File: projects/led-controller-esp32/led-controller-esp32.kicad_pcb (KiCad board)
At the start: 2 copper layers, 49.5 x 41 mm, 9 parts, among them J1 Conn_01x02, J2 LED PIGTAIL, U1 XIAO ESP32C3, U2 DC Buck 5V

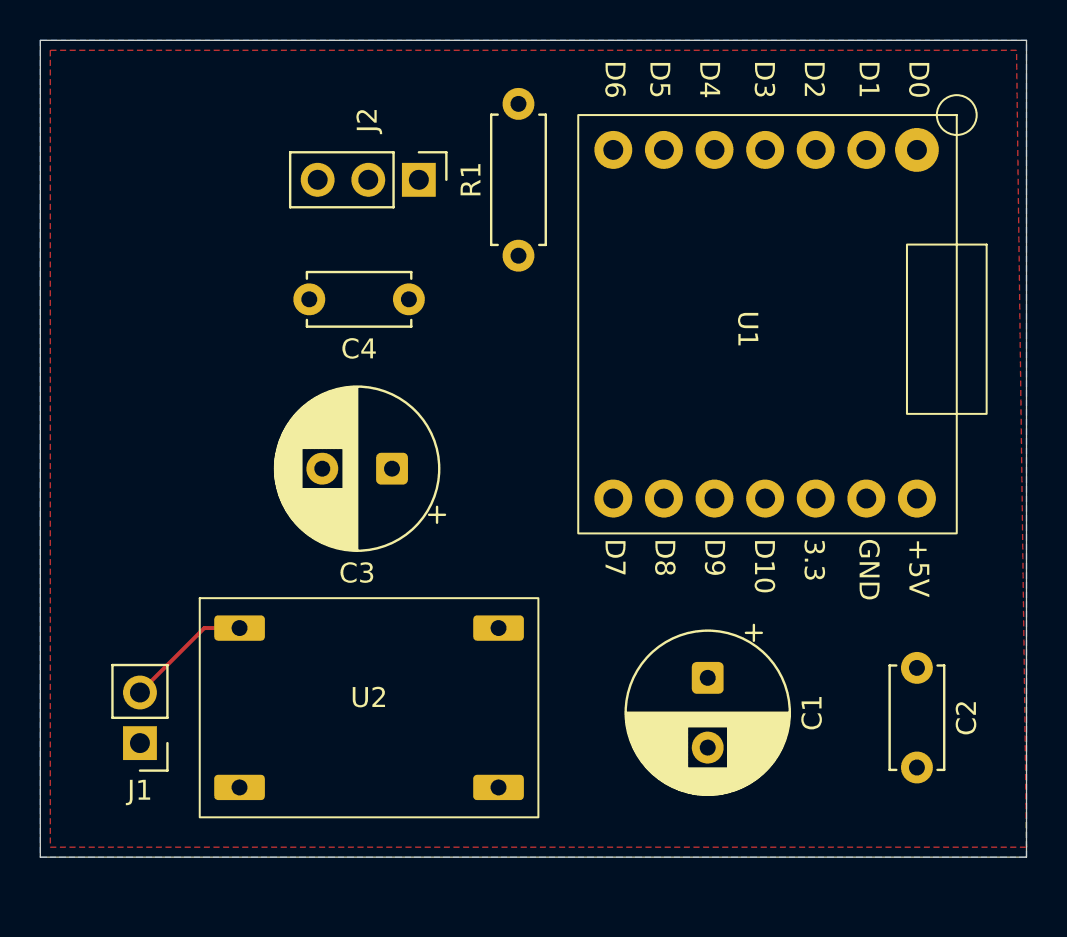
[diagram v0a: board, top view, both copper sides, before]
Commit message: use standard 2 screw terminal and other tidy ups
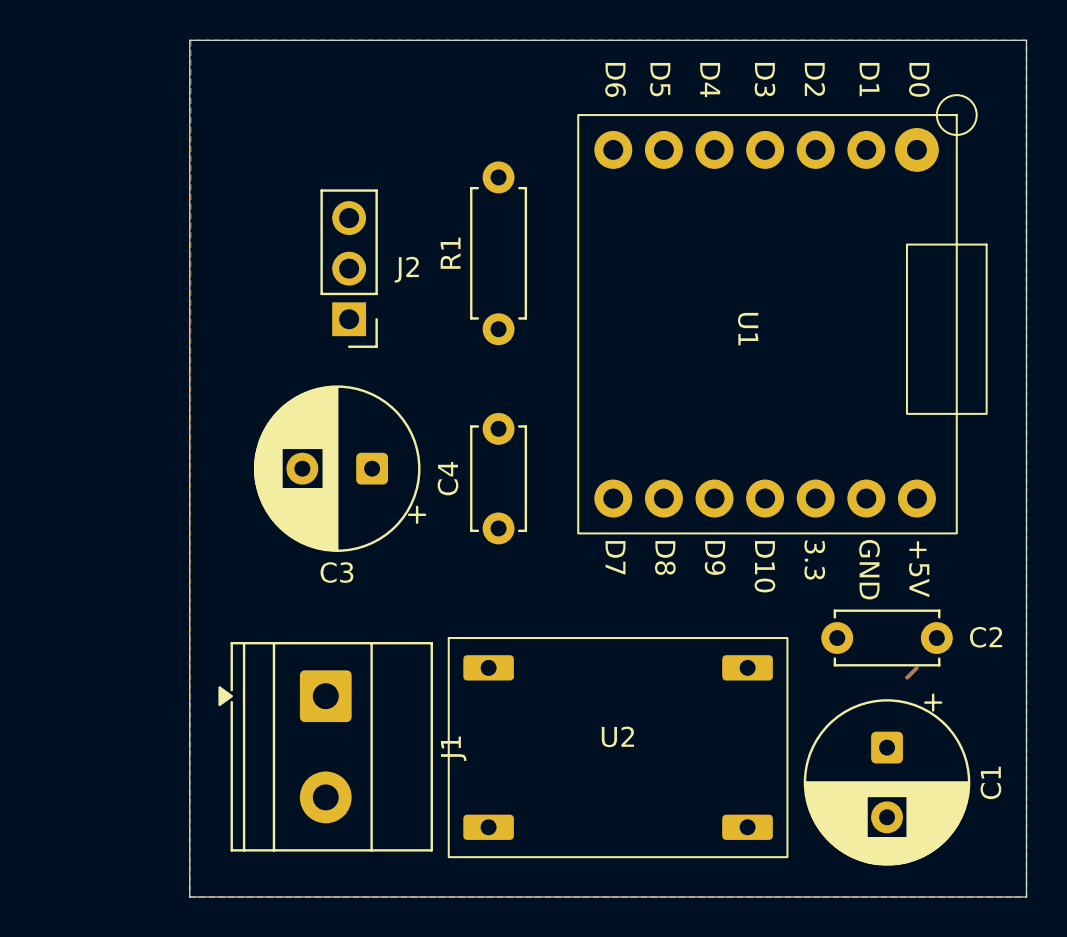
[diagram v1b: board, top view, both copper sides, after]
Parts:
- J1: value Conn_01x02 -> Screw_Terminal_01x02; footprint Connector_PinHeader_2.54mm:PinHeader_1x02_P2.54mm_Vertical -> TerminalBlock_Phoenix:TerminalBlock_Phoenix_MKDS-1,5-2-5.08_1x02_P5.08mm_Horizontal
- moved U2 12.7 mm to (106.0, 88.5)
- moved C4 12.3 mm to (100.0, 77.5), turned to 90 degrees
- moved C1 9.66 mm to (119.5, 88.5)
- moved J1 9.62 mm to (91.3, 85.9), turned to -90 degrees
- moved J2 7.83 mm to (92.5, 67.0), turned to 180 degrees
- moved C2 4.27 mm to (117.0, 83.0), turned to 0 degrees
- moved R1 3.82 mm to (100.0, 67.5)
- moved C3 1.00 mm to (93.7, 74.5)
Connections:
- J1 pad 1: GND -> +Vin
- J1 pad 2: +Vin -> GND
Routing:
- net +Vin: track 6.34 -> 0.00 mm
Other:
- board size 49.5 x 41 mm -> 42 x 43 mm

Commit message: label terminal blocks and other cleanups
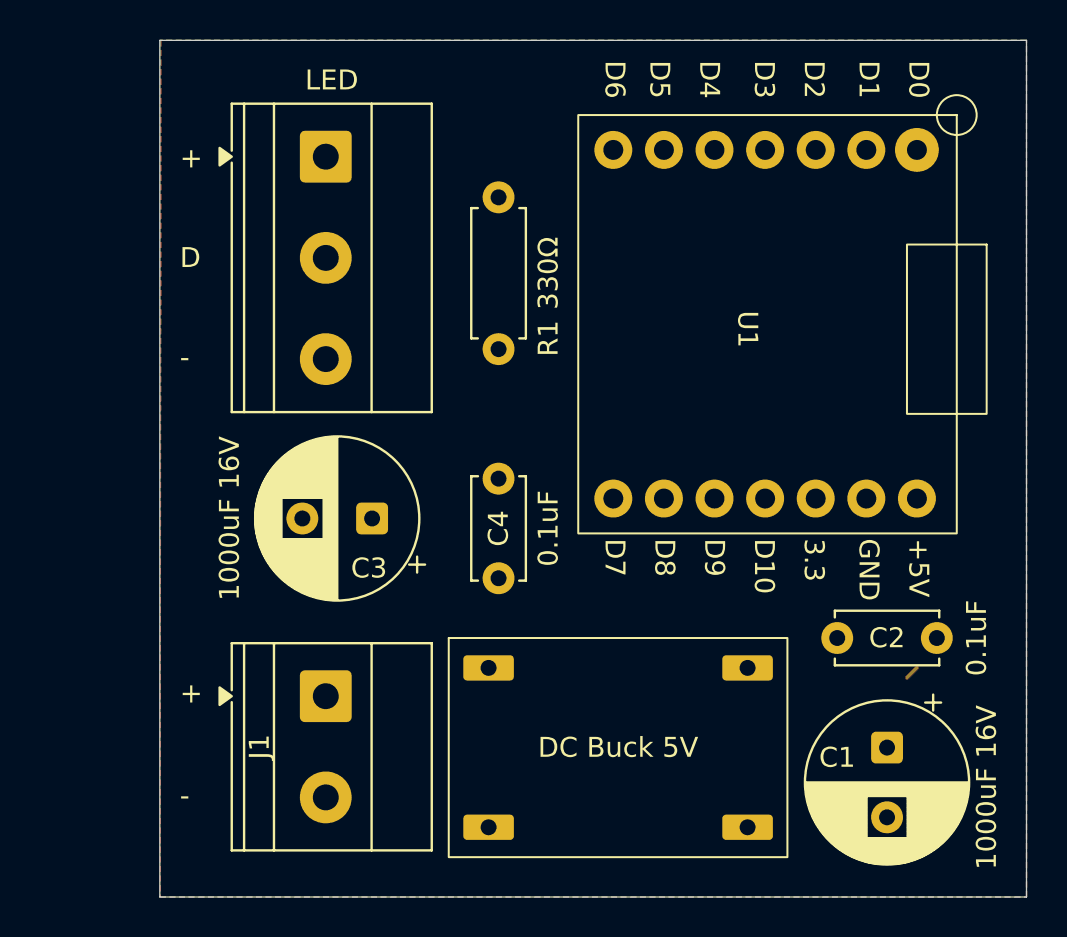
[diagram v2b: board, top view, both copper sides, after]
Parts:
- J2: value LED PIGTAIL -> LED; footprint Connector_PinHeader_2.54mm:PinHeader_1x03_P2.54mm_Vertical -> TerminalBlock_Phoenix:TerminalBlock_Phoenix_MKDS-1,5-3-5.08_1x03_P5.08mm_Horizontal
- moved J2 8.24 mm to (91.3, 58.8), turned to -90 degrees
- moved C3 2.50 mm to (93.7, 77.0)
- moved C4 2.50 mm to (100.0, 80.0)
- moved R1 1.00 mm to (100.0, 68.5)
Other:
- board size 42 x 43 mm -> 43.5 x 43 mm
- board text added: "+"
- board text added: "-"
- board text added: "D"
